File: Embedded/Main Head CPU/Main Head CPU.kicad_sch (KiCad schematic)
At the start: 47 parts, among them J1 10171746-00021LF, J10 Fan 1, J11 Substructure Power, J12 Head Power, J13 MicroSD, J2 Maw, J3 Tongue, J4 Left Fin, J5 Right Fin, J6 Scales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

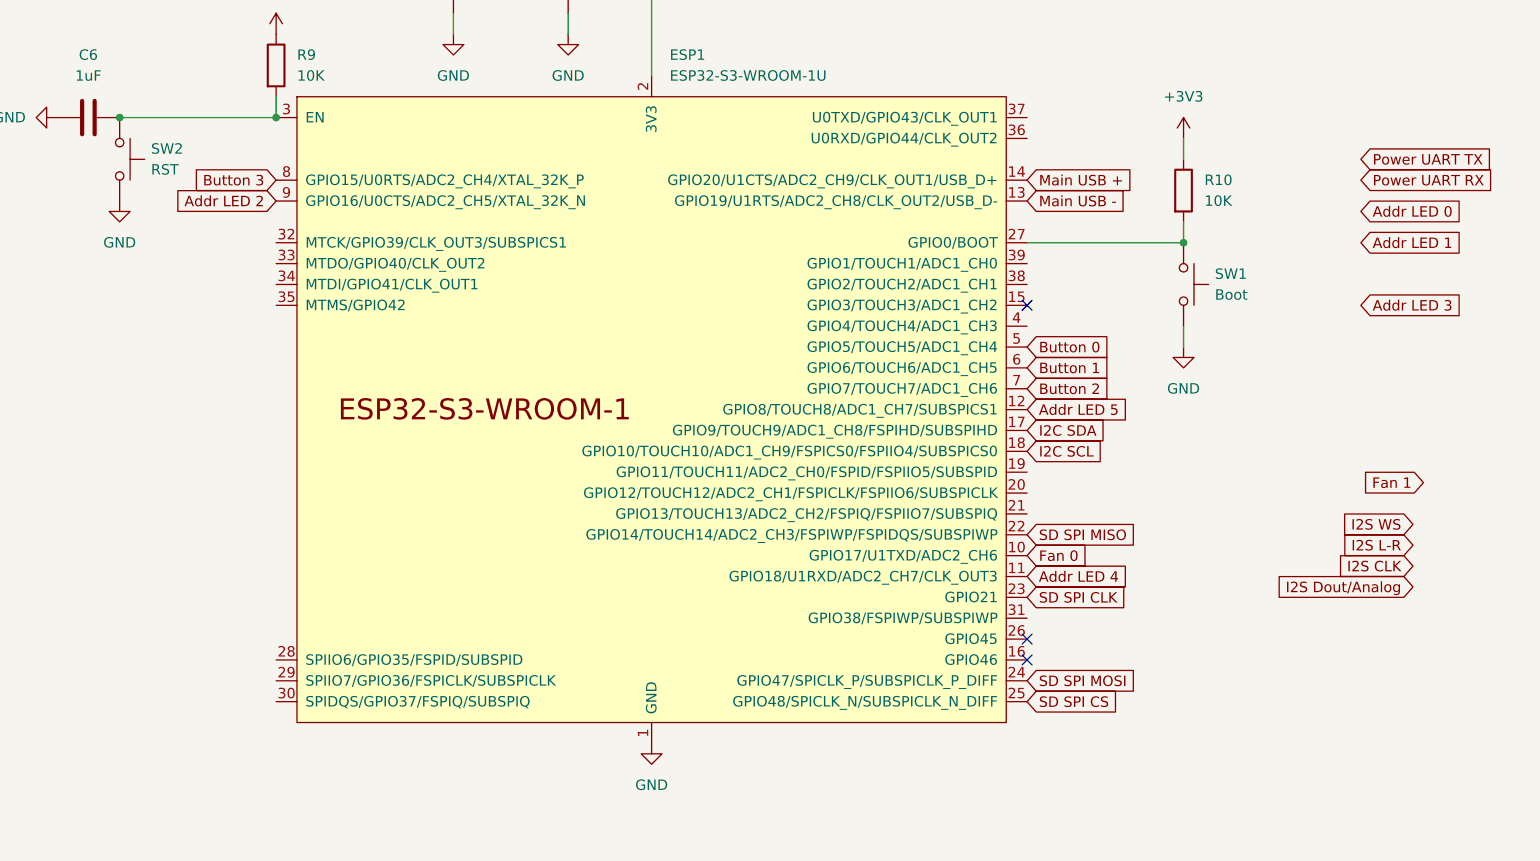
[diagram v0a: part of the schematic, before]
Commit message: Added Routing for all pins and pads
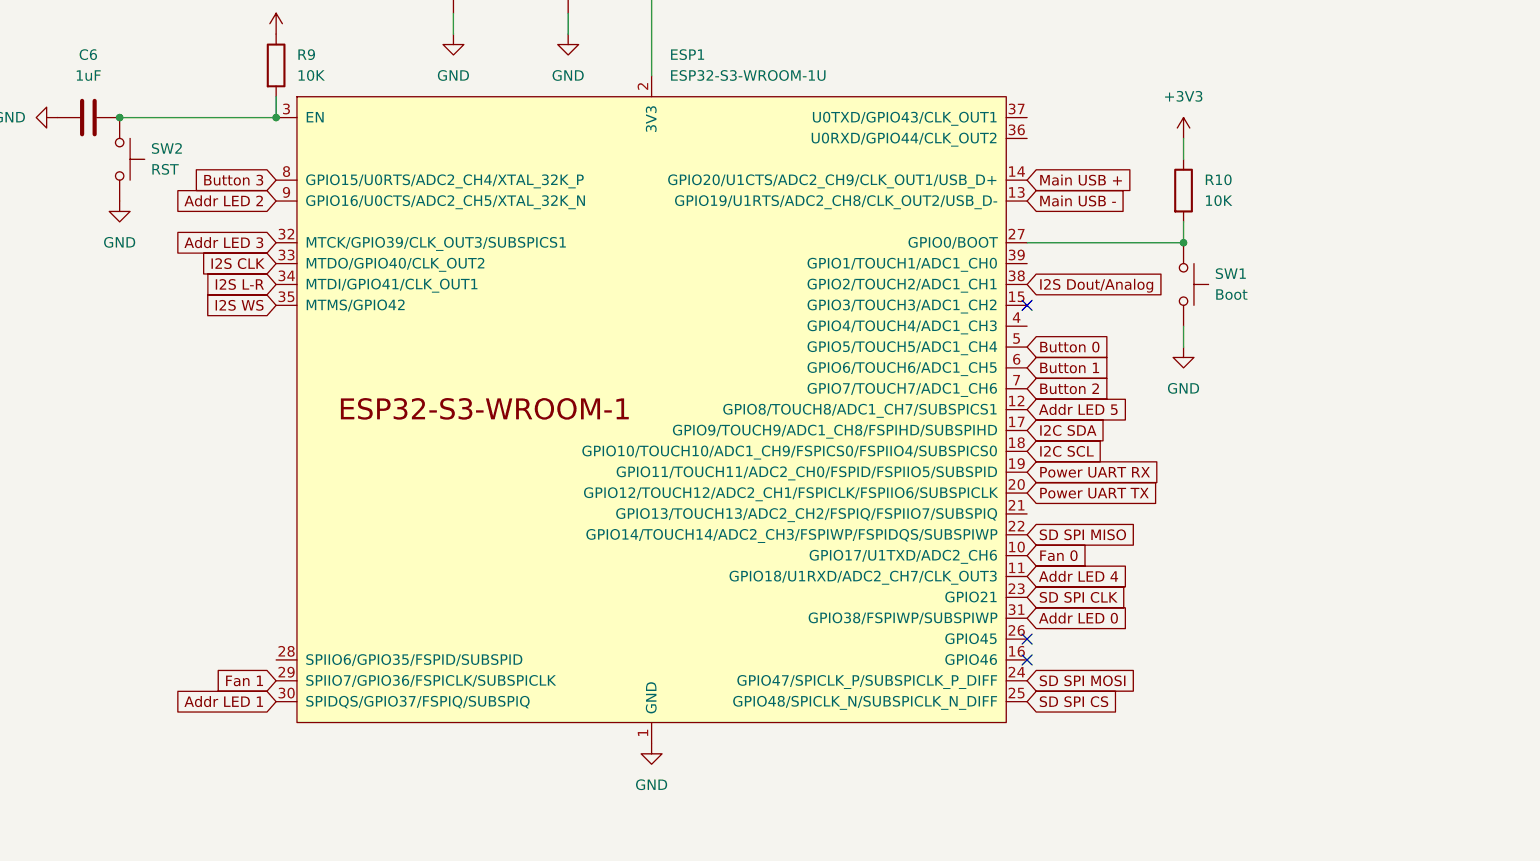
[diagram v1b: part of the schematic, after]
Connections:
- net Addr LED 0: now also ESP1.31 (GPIO38/FSPIWP/SUBSPIWP)
- net Addr LED 1: now also ESP1.30 (SPIDQS/GPIO37/FSPIQ/SUBSPIQ)
- net Addr LED 3: now also ESP1.32 (MTCK/GPIO39/CLK_OUT3/SUBSPICS1)
- net Fan 1: now also ESP1.29 (SPIIO7/GPIO36/FSPICLK/SUBSPICLK)
- net I2S CLK: now also ESP1.33 (MTDO/GPIO40/CLK_OUT2)
- net I2S Dout/Analog: now also ESP1.38 (GPIO2/TOUCH2/ADC1_CH1)
- net I2S L-R: now also ESP1.34 (MTDI/GPIO41/CLK_OUT1)
- net I2S WS: now also ESP1.35 (MTMS/GPIO42)
- net Power UART RX: now also ESP1.19 (GPIO11/TOUCH11/ADC2_CH0/FSPID/FSPIIO5/SUBSPID)
- net Power UART TX: now also ESP1.20 (GPIO12/TOUCH12/ADC2_CH1/FSPICLK/FSPIIO6/SUBSPICLK)
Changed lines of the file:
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@@
 	(global_label "Power UART RX"
 		(shape input)
-		(at 414.02 59.69 0)
-		(fields_autoplaced yes)
-		(effects
-			(font
-				(size 1.27 1.27)
-			)
-			(justify left)
-		)
-		(property "Intersheetrefs" "${INTERSHEET_REFS}"
-			(at 431.7009 59.69 0)
+		(at 373.38 95.25 0)
+		(fields_autoplaced yes)
+		(effects
+			(font
+				(size 1.27 1.27)
+			)
+			(justify left)
+		)
+		(property "Intersheetrefs" "${INTERSHEET_REFS}"
+			(at 391.0609 95.25 0)
 			(effects
 				(font
@@
 	(global_label "Addr LED 0"
 		(shape input)
-		(at 414.02 63.5 0)
-		(fields_autoplaced yes)
-		(effects
-			(font
-				(size 1.27 1.27)
-			)
-			(justify left)
-		)
-		(property "Intersheetrefs" "${INTERSHEET_REFS}"
-			(at 427.7698 63.5 0)
+		(at 373.38 113.03 0)
+		(fields_autoplaced yes)
+		(effects
+			(font
+				(size 1.27 1.27)
+			)
+			(justify left)
+		)
+		(property "Intersheetrefs" "${INTERSHEET_REFS}"
+			(at 387.1298 113.03 0)
 			(effects
 				(font
@@
 	(global_label "I2S L-R"
 		(shape input)
-		(at 420.37 104.14 180)
-		(fields_autoplaced yes)
-		(effects
-			(font
-				(size 1.27 1.27)
-			)
-			(justify right)
-		)
-		(property "Intersheetrefs" "${INTERSHEET_REFS}"
-			(at 409.5229 104.14 0)
+		(at 281.94 72.39 180)
+		(fields_autoplaced yes)
+		(effects
+			(font
+				(size 1.27 1.27)
+			)
+			(justify right)
+		)
+		(property "Intersheetrefs" "${INTERSHEET_REFS}"
+			(at 271.0929 72.39 0)
 			(effects
 				(font
@@
 	(global_label "I2S Dout{slash}Analog"
 		(shape input)
-		(at 420.37 109.22 180)
-		(fields_autoplaced yes)
-		(effects
-			(font
-				(size 1.27 1.27)
-			)
-			(justify right)
-		)
-		(property "Intersheetrefs" "${INTERSHEET_REFS}"
-			(at 401.4194 109.22 0)
-			(effects
-				(font
-					(size 1.27 1.27)
-				)
-				(justify right)
+		(at 373.38 72.39 0)
+		(fields_autoplaced yes)
+		(effects
+			(font
+				(size 1.27 1.27)
+			)
+			(justify left)
+		)
+		(property "Intersheetrefs" "${INTERSHEET_REFS}"
+			(at 392.3306 72.39 0)
+			(effects
+				(font
+					(size 1.27 1.27)
+				)
+				(justify left)
 				(hide yes)
 			)
@@
 	(global_label "Addr LED 3"
 		(shape input)
-		(at 414.02 74.93 0)
-		(fields_autoplaced yes)
-		(effects
-			(font
-				(size 1.27 1.27)
-			)
-			(justify left)
-		)
-		(property "Intersheetrefs" "${INTERSHEET_REFS}"
-			(at 427.7698 74.93 0)
-			(effects
-				(font
-					(size 1.27 1.27)
-				)
-				(justify left)
+		(at 281.94 67.31 180)
+		(fields_autoplaced yes)
+		(effects
+			(font
+				(size 1.27 1.27)
+			)
+			(justify right)
+		)
+		(property "Intersheetrefs" "${INTERSHEET_REFS}"
+			(at 268.1902 67.31 0)
+			(effects
+				(font
+					(size 1.27 1.27)
+				)
+				(justify right)
 				(hide yes)
 			)
@@
 	(global_label "I2S CLK"
 		(shape input)
-		(at 420.37 106.68 180)
-		(fields_autoplaced yes)
-		(effects
-			(font
-				(size 1.27 1.27)
-			)
-			(justify right)
-		)
-		(property "Intersheetrefs" "${INTERSHEET_REFS}"
-			(at 409.8253 106.68 0)
+		(at 281.94 69.85 180)
+		(fields_autoplaced yes)
+		(effects
+			(font
+				(size 1.27 1.27)
+			)
+			(justify right)
+		)
+		(property "Intersheetrefs" "${INTERSHEET_REFS}"
+			(at 271.3953 69.85 0)
 			(effects
 				(font
@@
 	(global_label "Fan 1"
 		(shape input)
-		(at 421.64 96.52 180)
-		(fields_autoplaced yes)
-		(effects
-			(font
-				(size 1.27 1.27)
-			)
-			(justify right)
-		)
-		(property "Intersheetrefs" "${INTERSHEET_REFS}"
-			(at 413.0911 96.52 0)
+		(at 281.94 120.65 180)
+		(fields_autoplaced yes)
+		(effects
+			(font
+				(size 1.27 1.27)
+			)
+			(justify right)
+		)
+		(property "Intersheetrefs" "${INTERSHEET_REFS}"
+			(at 273.3911 120.65 0)
 			(effects
 				(font
@@
 	(global_label "I2S WS"
 		(shape input)
-		(at 420.37 101.6 180)
-		(fields_autoplaced yes)
-		(effects
-			(font
-				(size 1.27 1.27)
-			)
-			(justify right)
-		)
-		(property "Intersheetrefs" "${INTERSHEET_REFS}"
-			(at 410.7325 101.6 0)
+		(at 281.94 74.93 180)
+		(fields_autoplaced yes)
+		(effects
+			(font
+				(size 1.27 1.27)
+			)
+			(justify right)
+		)
+		(property "Intersheetrefs" "${INTERSHEET_REFS}"
+			(at 272.3025 74.93 0)
 			(effects
 				(font
@@
 	(global_label "Addr LED 1"
 		(shape input)
-		(at 414.02 67.31 0)
-		(fields_autoplaced yes)
-		(effects
-			(font
-				(size 1.27 1.27)
-			)
-			(justify left)
-		)
-		(property "Intersheetrefs" "${INTERSHEET_REFS}"
-			(at 427.7698 67.31 0)
-			(effects
-				(font
-					(size 1.27 1.27)
-				)
-				(justify left)
+		(at 281.94 123.19 180)
+		(fields_autoplaced yes)
+		(effects
+			(font
+				(size 1.27 1.27)
+			)
+			(justify right)
+		)
+		(property "Intersheetrefs" "${INTERSHEET_REFS}"
+			(at 268.1902 123.19 0)
+			(effects
+				(font
+					(size 1.27 1.27)
+				)
+				(justify right)
 				(hide yes)
 			)
@@
 	(global_label "Power UART TX"
 		(shape input)
-		(at 414.02 57.15 0)
-		(fields_autoplaced yes)
-		(effects
-			(font
-				(size 1.27 1.27)
-			)
-			(justify left)
-		)
-		(property "Intersheetrefs" "${INTERSHEET_REFS}"
-			(at 431.3985 57.15 0)
-			(effects
-				(font
+		(at 373.38 97.79 0)
+		(fields_autoplaced yes)
+		(effects
+			(font
+				(size 1.27 1.27)
+			)
+			(justify left)
+		)
+		(property "Intersheetrefs" "${INTERSHEET_REFS}"
+			(at 390.7585 97.79 0)
+			(effects
+				(font

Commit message: Modified Routing & Silkscreen
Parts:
- removed J8: Conn_01x06, Connector_PinHeader_2.54mm:PinHeader_1x06_P2.54mm_Vertical, symbol Connector_Generic:Conn_01x06
- removed U2: Buttons, FCC:FFC 0.8mm 8P, symbol FFC:FFC-8
- added J14: Mic, Connector_JST:JST_GH_SM08B-GHS-TB_1x08-1MP_P1.25mm_Horizontal, symbol Connector:Conn_01x08_Socket
- added J15: I2C, Connector_JST:JST_GH_SM08B-GHS-TB_1x08-1MP_P1.25mm_Horizontal, symbol Connector:Conn_01x08_Socket
- added J8: Buttons, Connector_JST:JST_GH_SM08B-GHS-TB_1x08-1MP_P1.25mm_Horizontal, symbol Connector:Conn_01x08_Socket
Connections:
- net +3V3: now also J15.4 (Pin_4), J15.5 (Pin_5), J8.4 (Pin_4), J8.5 (Pin_5)
- net Button 0: now also J8.2 (Pin_2)
- net Button 1: now also J8.3 (Pin_3)
- net Button 2: now also J8.6 (Pin_6)
- net Button 3: now also J8.7 (Pin_7)
- net GND: now also J14.1 (Pin_1), J14.8 (Pin_8), J15.1 (Pin_1), J15.8 (Pin_8), J8.1 (Pin_1), J8.8 (Pin_8)
- net I2C SCL: now also J15.3 (Pin_3), J15.7 (Pin_7)
- net I2C SDA: now also J15.2 (Pin_2), J15.6 (Pin_6)
- net I2S CLK: now also J14.3 (Pin_3)
- net I2S Dout/Analog: now also J14.2 (Pin_2)
- net I2S L-R: now also J14.6 (Pin_6)
- net I2S WS: now also J14.7 (Pin_7)
- net at JP1.2 (C): now also J14.4 (Pin_4), J14.5 (Pin_5)
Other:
- moved on the sheet: JP1, U1

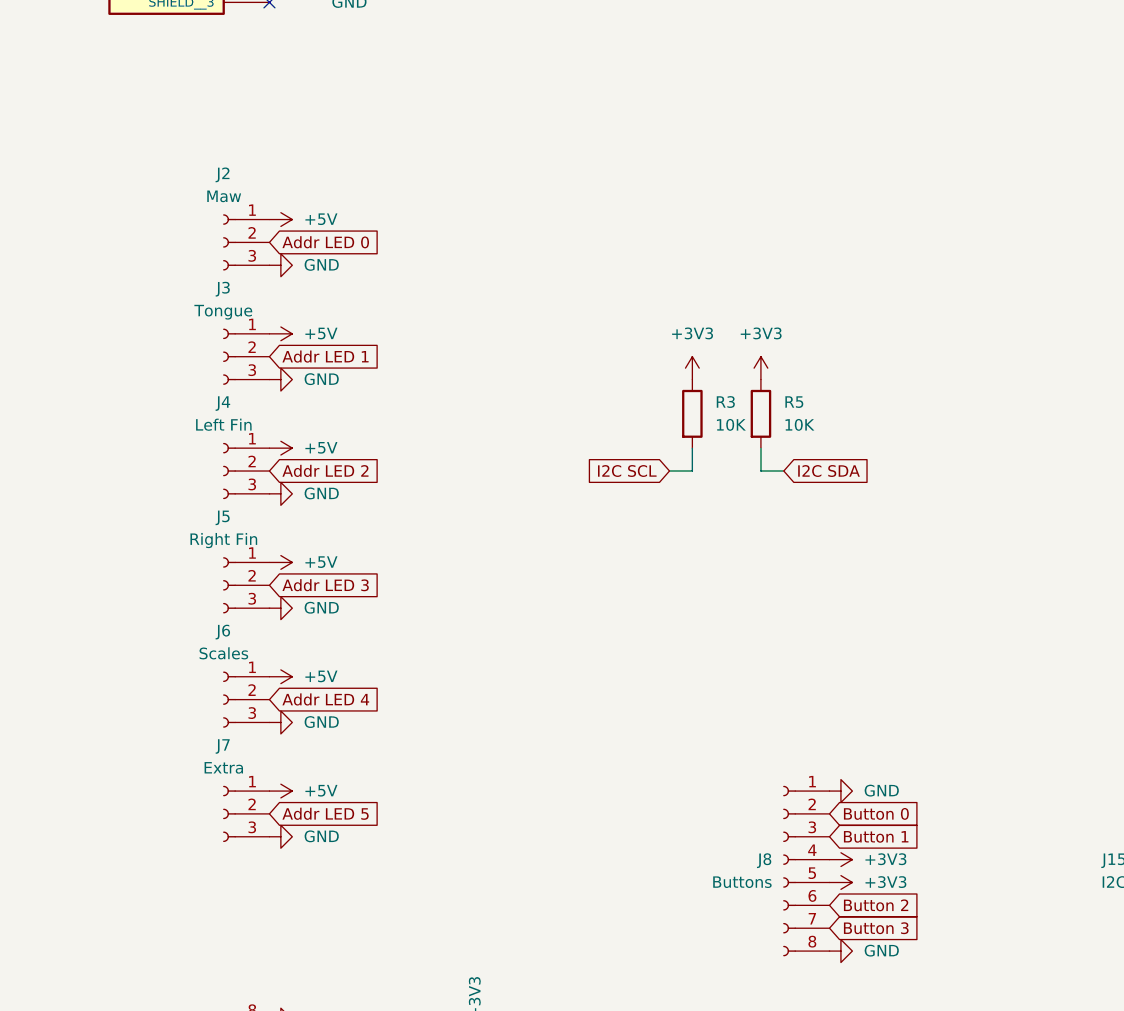
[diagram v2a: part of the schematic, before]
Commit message: Modified Addressable LED strip labels for general systems
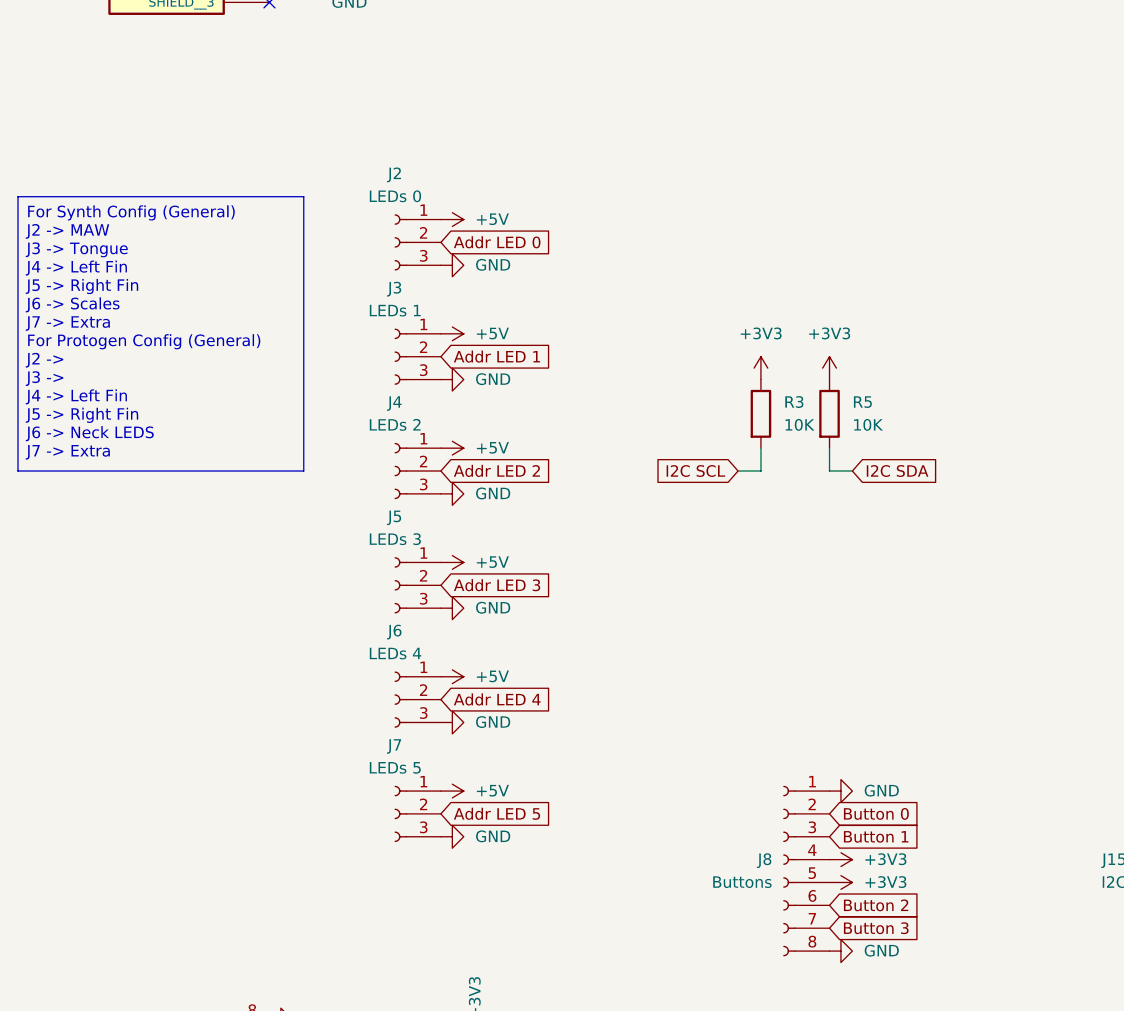
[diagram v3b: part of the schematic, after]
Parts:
- J2: value Maw -> LEDs 0
- J3: value Tongue -> LEDs 1
- J4: value Left Fin -> LEDs 2
- J5: value Right Fin -> LEDs 3
- J6: value Scales -> LEDs 4
- J7: value Extra -> LEDs 5
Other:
- moved on the sheet: J2, J3, J4, J5, J6, J7, R3, R5

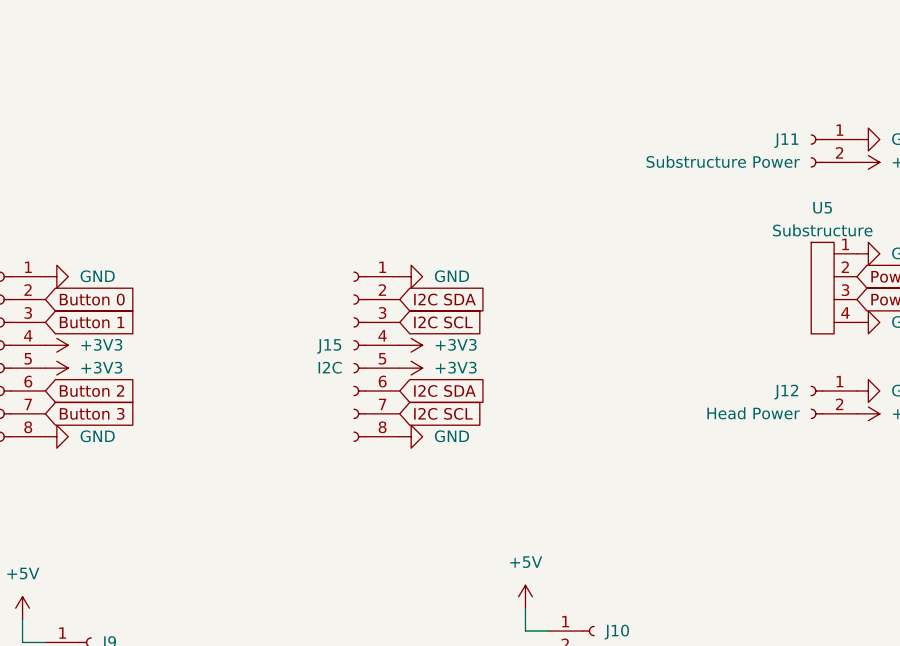
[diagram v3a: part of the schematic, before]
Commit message: Added Pull down resistors to buttons
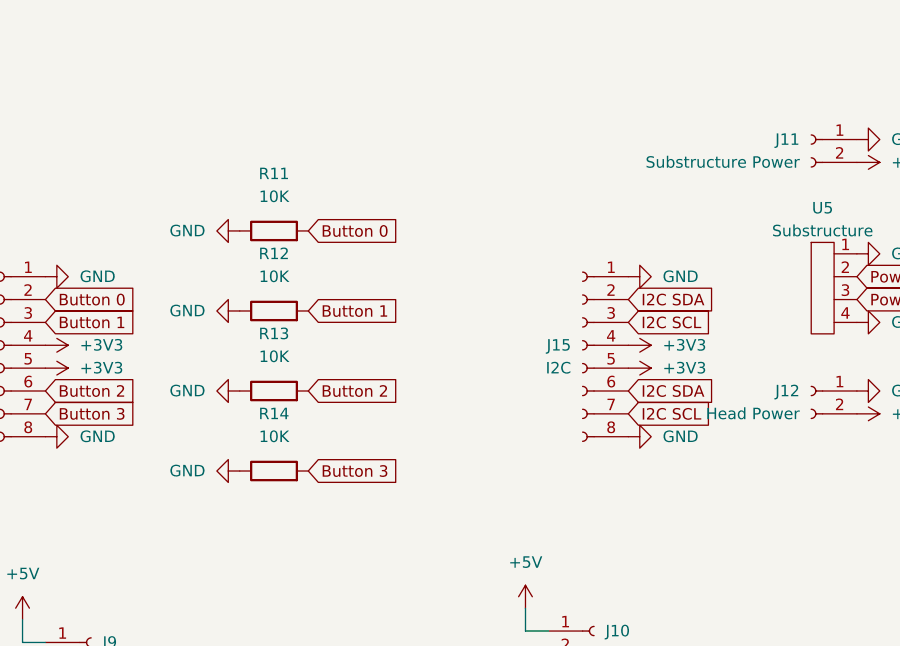
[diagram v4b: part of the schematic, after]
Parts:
- added R11, R12, R13, R14: 10K, Resistor_SMD:R_0603_1608Metric_Pad0.98x0.95mm_HandSolder, symbol Device:R
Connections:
- net Button 0: now also R11.2
- net Button 1: now also R12.2
- net Button 2: now also R13.2
- net Button 3: now also R14.2
- net GND: now also R11.1, R12.1, R13.1, R14.1
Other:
- moved on the sheet: J15

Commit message: Modified Addressable LED ports for general (instead of static config names)
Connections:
- net Addr LED 0: now also ESP1.9 (GPIO16/U0CTS/ADC2_CH5/XTAL_32K_N); no longer ESP1.31 (GPIO38/FSPIWP/SUBSPIWP)
- net Addr LED 1: now also ESP1.11 (GPIO18/U1RXD/ADC2_CH7/CLK_OUT3); no longer ESP1.30 (SPIDQS/GPIO37/FSPIQ/SUBSPIQ)
- net Addr LED 2: now also ESP1.12 (GPIO8/TOUCH8/ADC1_CH7/SUBSPICS1); no longer ESP1.9 (GPIO16/U0CTS/ADC2_CH5/XTAL_32K_N)
- net Addr LED 4: now also ESP1.31 (GPIO38/FSPIWP/SUBSPIWP); no longer ESP1.11 (GPIO18/U1RXD/ADC2_CH7/CLK_OUT3)
- net Addr LED 5: now also ESP1.30 (SPIDQS/GPIO37/FSPIQ/SUBSPIQ); no longer ESP1.12 (GPIO8/TOUCH8/ADC1_CH7/SUBSPICS1)
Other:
- moved on the sheet: J2, J3, J4, J5, J6, J7
